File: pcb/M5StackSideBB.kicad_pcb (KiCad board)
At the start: 2 copper layers, 100 x 50 mm, 15 parts, among them J1 Conn_01x11, J2 Conn_01x11, J3 Conn_02x15_Odd_Even, J4 Conn_02x15_Odd_Even

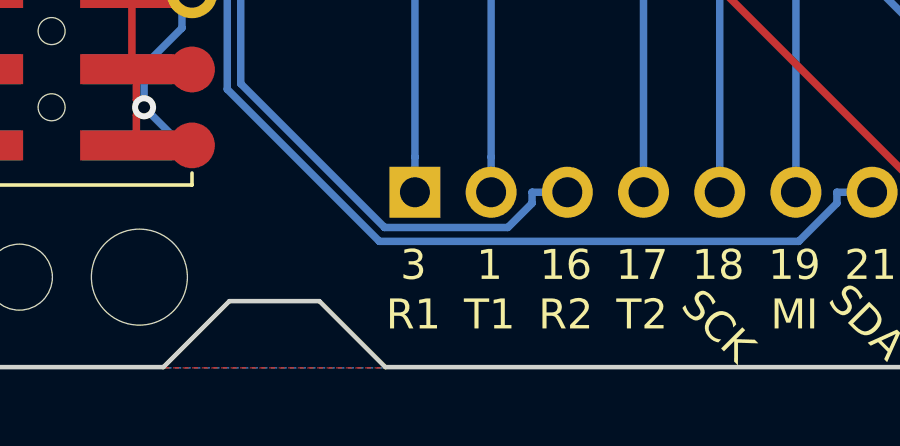
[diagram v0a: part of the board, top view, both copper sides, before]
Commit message: Correct UART number for G1 and G3
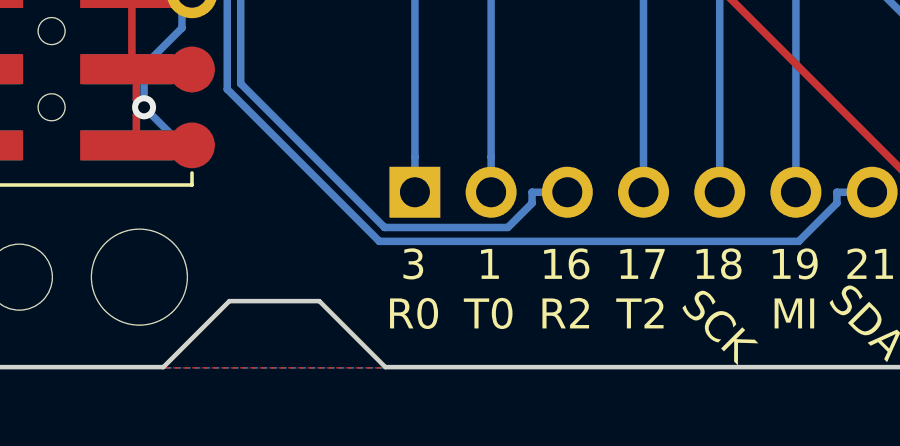
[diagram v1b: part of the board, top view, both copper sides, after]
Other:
- board text added: "R0"
- board text added: "T0"
- board text removed: "R1"
- board text removed: "T1"
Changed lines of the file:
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@@
   (gr_line (start 153 97.8) (end 155.2 100) (layer Edge.Cuts) (width 0.15))
   (gr_line (start 150 97.8) (end 153 97.8) (layer Edge.Cuts) (width 0.15))
-  (gr_text R1 (at 156.1338 98.2472) (layer F.SilkS)
+  (gr_text R0 (at 156.1338 98.2472) (layer F.SilkS)
     (effects (font (size 1 1) (thickness 0.25)))
   )
-  (gr_text T1 (at 158.6738 98.2472) (layer F.SilkS)
+  (gr_text T0 (at 158.6738 98.2472) (layer F.SilkS)
     (effects (font (size 1 1) (thickness 0.25)))
   )

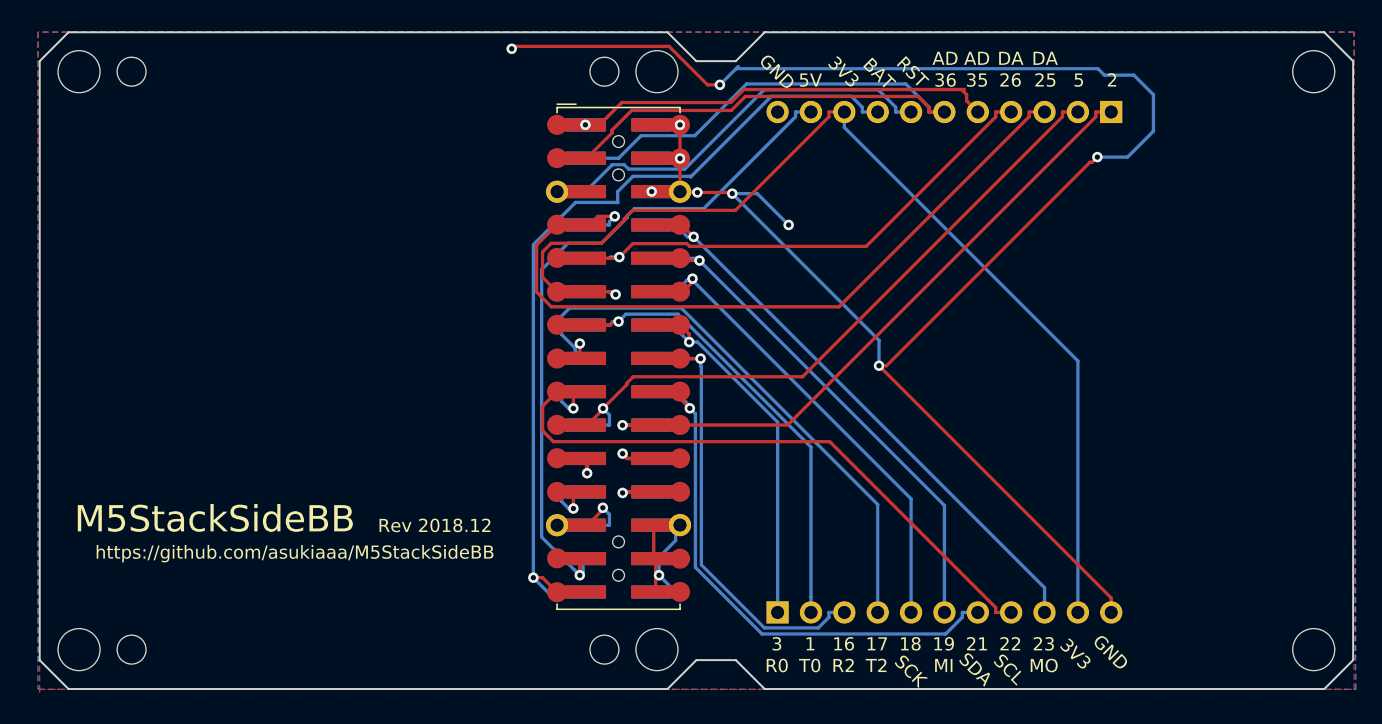
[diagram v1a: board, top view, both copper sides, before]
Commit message: Use 14 pins headers
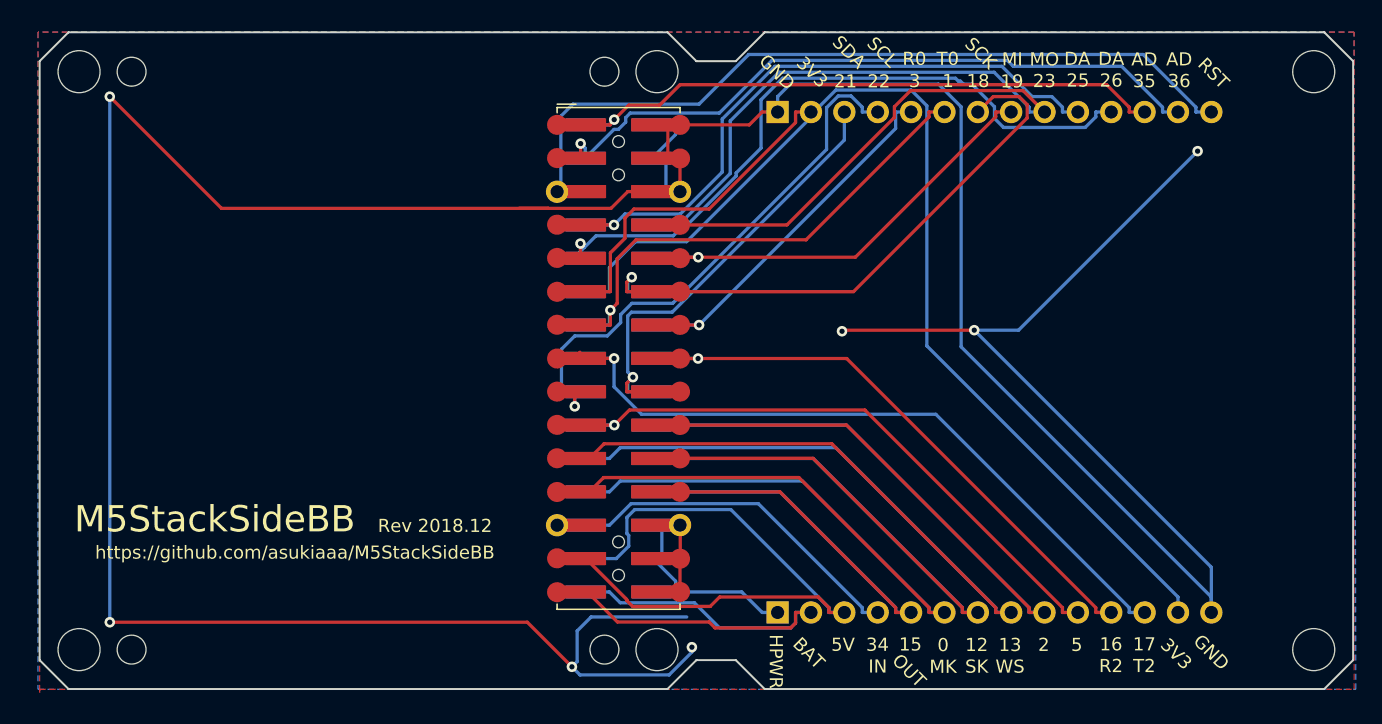
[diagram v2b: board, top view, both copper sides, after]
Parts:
- removed REF**: OSHW-Logo2_7.3x6mm_SilkScreen, Symbol:OSHW-Logo2_7.3x6mm_SilkScreen
- J1, J2: value Conn_01x11 -> Conn_01x14; footprint footprints:PinSocket_1x11_P2.54mm_Vertical_without_silk -> footprints:PinSocket_1x14_P2.54mm_Vertical_without_silk
- moved J1 25.4 mm to (156.2, 56.1), turned to 90 degrees
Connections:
- J1 pad 1: G2 -> GND
- J1 pad 10: +5V -> G25
- J1 pad 11: GND -> G26
- J1 pad 2: G5 -> +3V3
- J1 pad 3: G25 -> G21
- J1 pad 4: G26 -> G22
- J1 pad 5: G35 -> G3
- J1 pad 6: G36 -> G1
- J1 pad 7: RST -> G18
- J1 pad 8: +BATT -> G19
- J1 pad 9: +3V3 -> G23
- J2 pad 1: G3 -> HPWR
- J2 pad 10: +3V3 -> G5
- J2 pad 11: GND -> G16
- J2 pad 2: G1 -> +BATT
- J2 pad 3: G16 -> +5V
- J2 pad 4: G17 -> G34
- J2 pad 5: G18 -> G15
- J2 pad 6: G19 -> G0
- J2 pad 7: G21 -> G12
- J2 pad 8: G22 -> G13
- J2 pad 9: G23 -> G2
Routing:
- net GND: track 154.9 -> 302.8 mm, vias 10 -> 7
- net G13: track 4.77 -> 78.8 mm, vias 1 -> 0
- net G0: track 7.44 -> 66.5 mm, vias 1 -> 0
- net G12: track 7.24 -> 59.8 mm, vias 1 -> 0
- net G15: track 6.95 -> 47.5 mm, vias 1 -> 0
- net RST: track 33.5 -> 63.6 mm
- net G23: track 46.8 -> 73.8 mm, vias 1 -> 0
- net +BATT: track 66.7 -> 40.9 mm, vias 1 -> 0
- net +3V3: track 83.6 -> 109.0 mm, vias 1 -> 0
- net G34: track 7.63 -> 31.2 mm, vias 1 -> 0
- net G2: track 49.5 -> 72.1 mm, vias 1 -> 0
- net G35: track 34.4 -> 49.5 mm
- net G26: track 42.2 -> 56.5 mm
- net G17: track 46.8 -> 57.1 mm
- net G16: track 36.8 -> 46.7 mm
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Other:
- board text added: "0"
- board text added: "12"
- board text added: "13"
- board text added: "15"
- board text added: "34"
- board text added: "HPWR"
- board text added: "IN"
- board text added: "MK"
- board text added: "OUT"
- board text added: "SK"
- board text added: "WS"

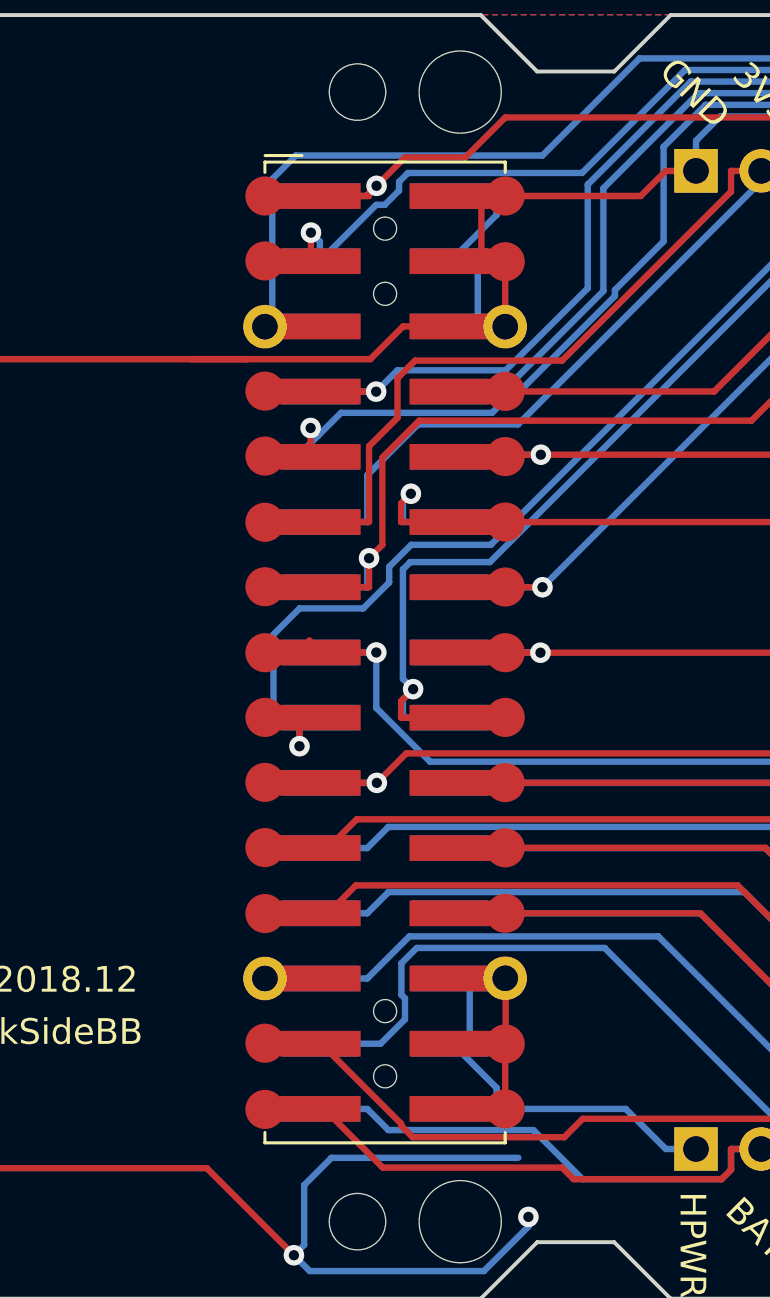
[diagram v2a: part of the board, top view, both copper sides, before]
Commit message: Remove redundant top pad
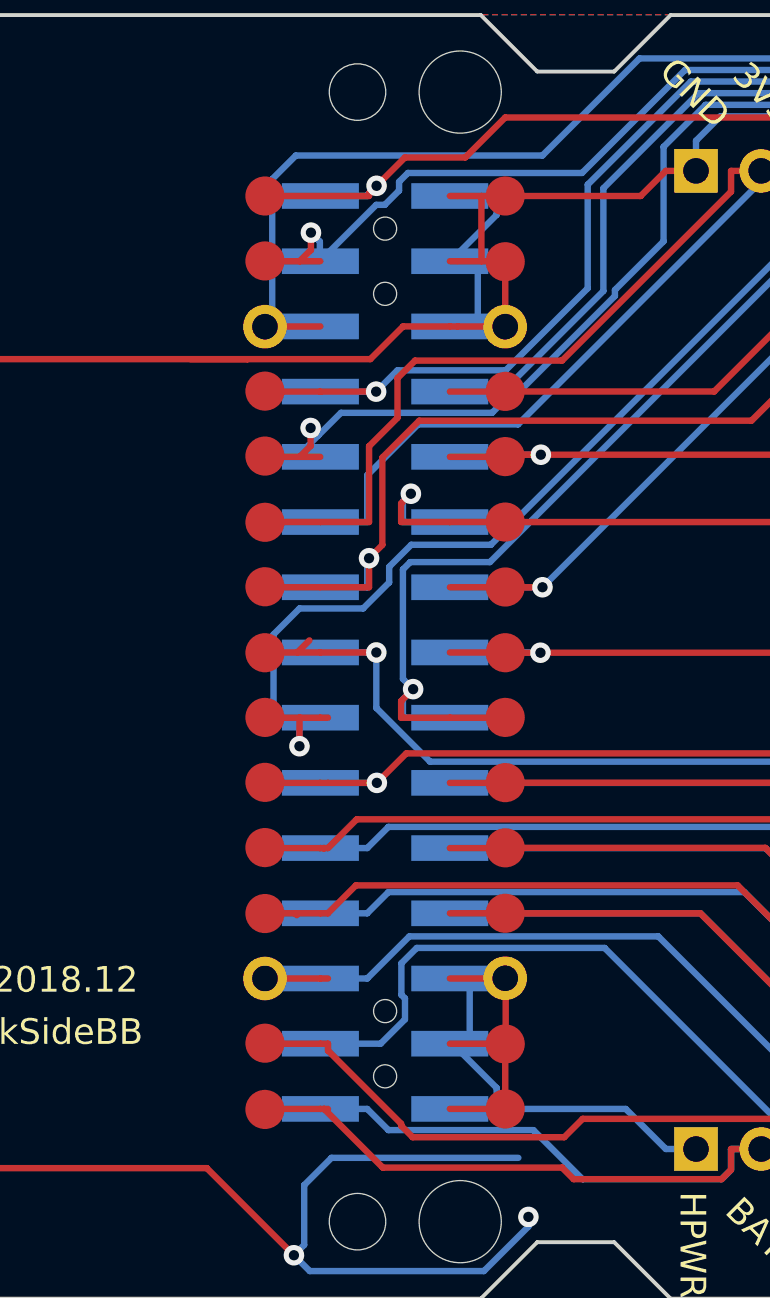
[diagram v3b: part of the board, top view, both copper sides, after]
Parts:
- J3: footprint footprints:PinHeader_2x15_P2.54mm_Vertical_SMD_for_M5Stack_top -> footprints:PinHeader_2x15_P2.54mm_Vertical_SMD_for_M5Stack_top_only_round_pads

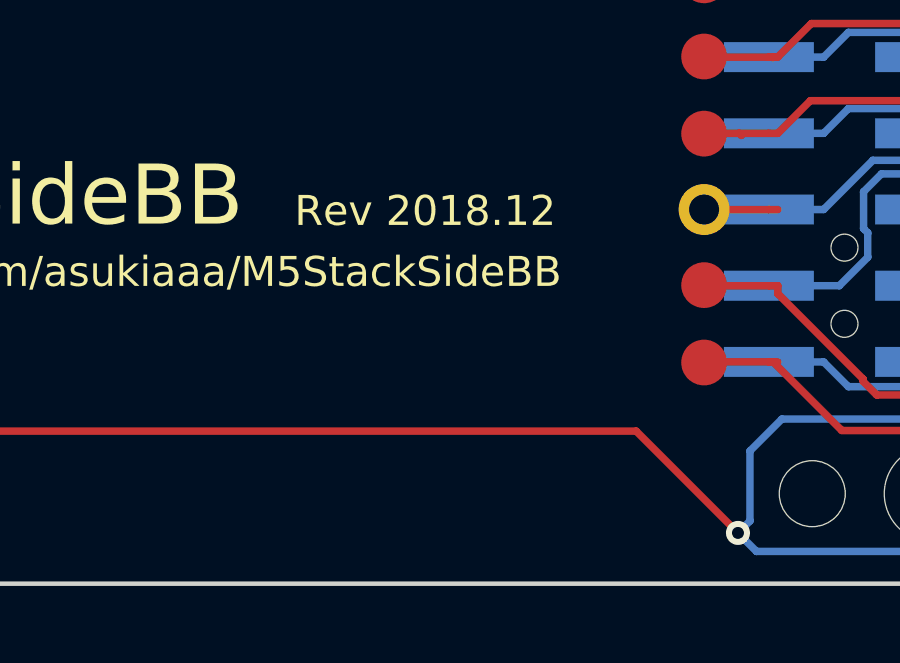
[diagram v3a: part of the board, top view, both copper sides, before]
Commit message: Update revision as 2019.01
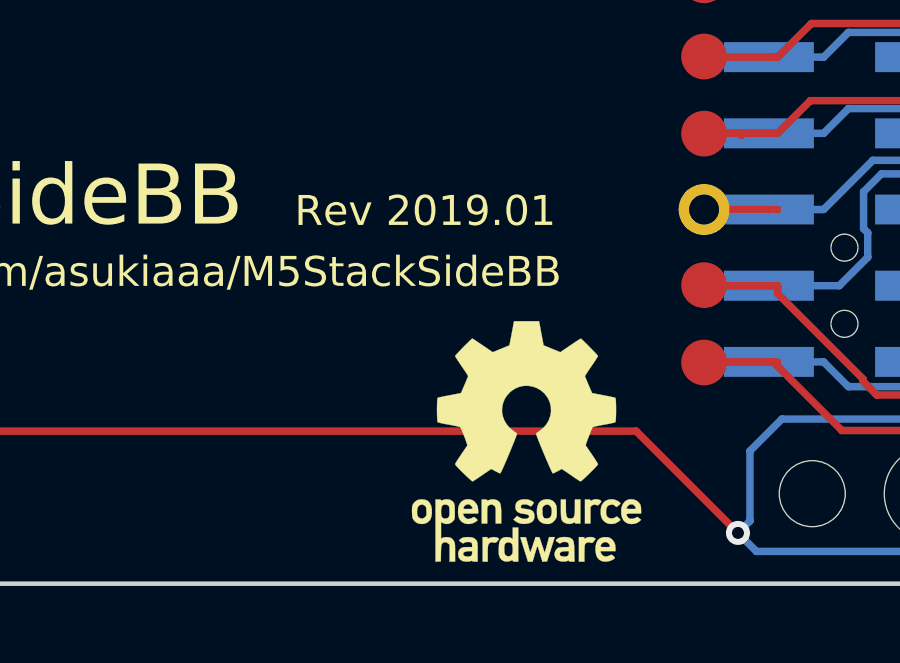
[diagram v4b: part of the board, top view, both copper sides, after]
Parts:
- added REF**: OSHW-Logo_7.5x8mm_SilkScreen, Symbol:OSHW-Logo_7.5x8mm_SilkScreen, F.Cu at (133.5, 95.3)
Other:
- board text added: "Rev 2019.01"
- board text removed: "Rev 2018.12"

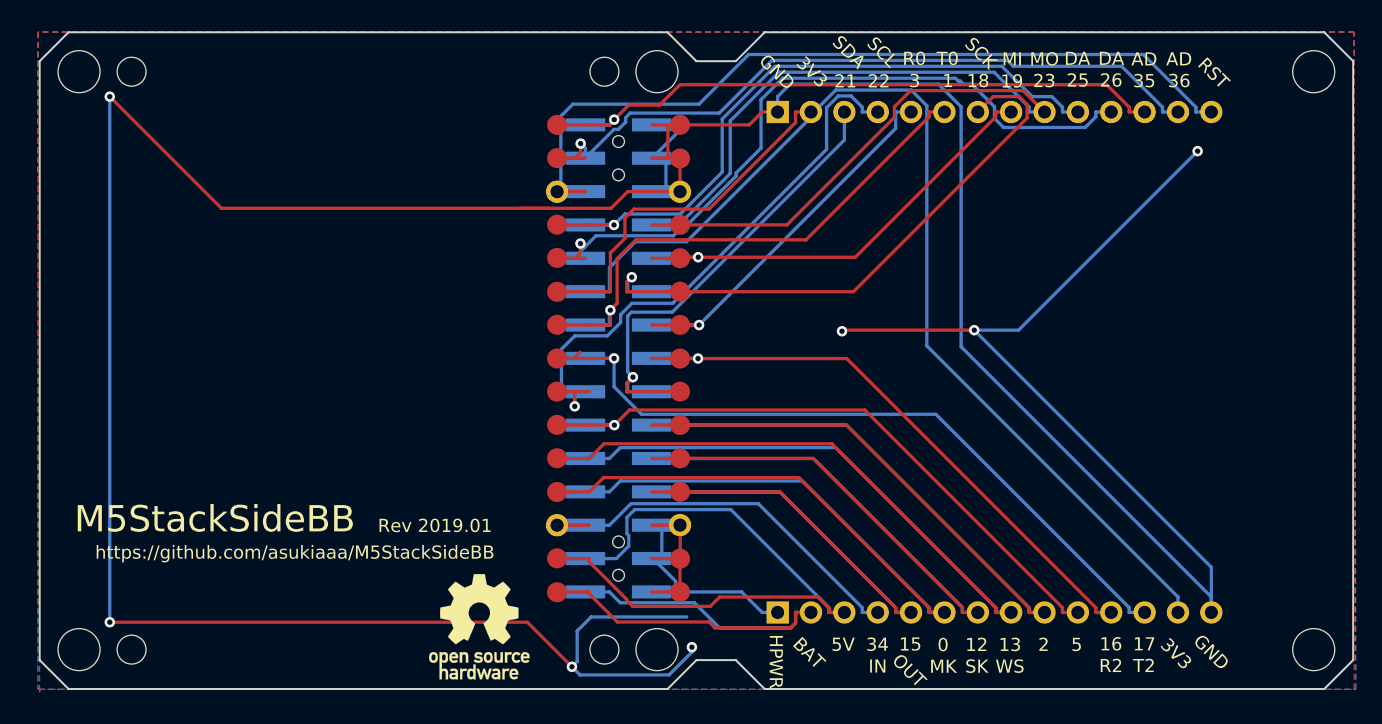
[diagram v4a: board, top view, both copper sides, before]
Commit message: Remove redundant wire
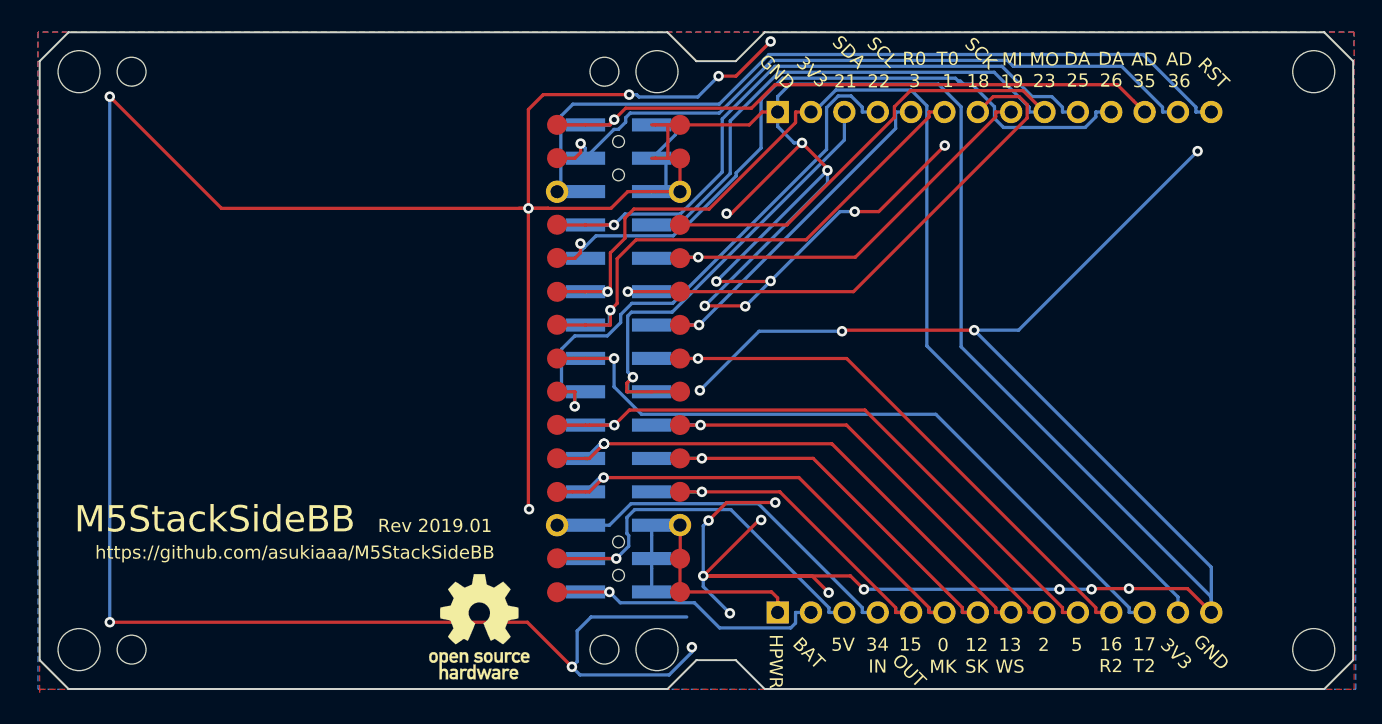
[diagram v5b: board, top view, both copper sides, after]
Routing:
- net GND: track 302.8 -> 504.6 mm, vias 7 -> 32
- net G13: track 78.8 -> 44.0 mm, vias 0 -> 2
- net G2: track 72.1 -> 37.6 mm, vias 0 -> 1
- net G0: track 66.5 -> 37.8 mm, vias 0 -> 1
- net G12: track 59.8 -> 33.1 mm, vias 0 -> 1
- net +3V3: track 109.0 -> 87.0 mm, vias 0 -> 1
- net G15: track 47.5 -> 27.0 mm, vias 0 -> 1
- net +5V: track 50.8 -> 30.7 mm, vias 0 -> 1
- net +BATT: track 40.9 -> 23.6 mm, vias 0 -> 1
- net HPWR: track 31.7 -> 23.5 mm
- net G18: track 45.8 -> 43.2 mm
- net G34: track 31.2 -> 28.7 mm
- net G19: track 35.8 -> 33.6 mm
- net G16: track 46.7 -> 44.6 mm
- net G23: track 73.8 -> 71.7 mm
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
